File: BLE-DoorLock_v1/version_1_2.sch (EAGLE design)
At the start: 33 parts, among them K1 G5LE-14_DC12, Q1 MMBT2222, Q2 MMBT2222, Q3 DMN6140L

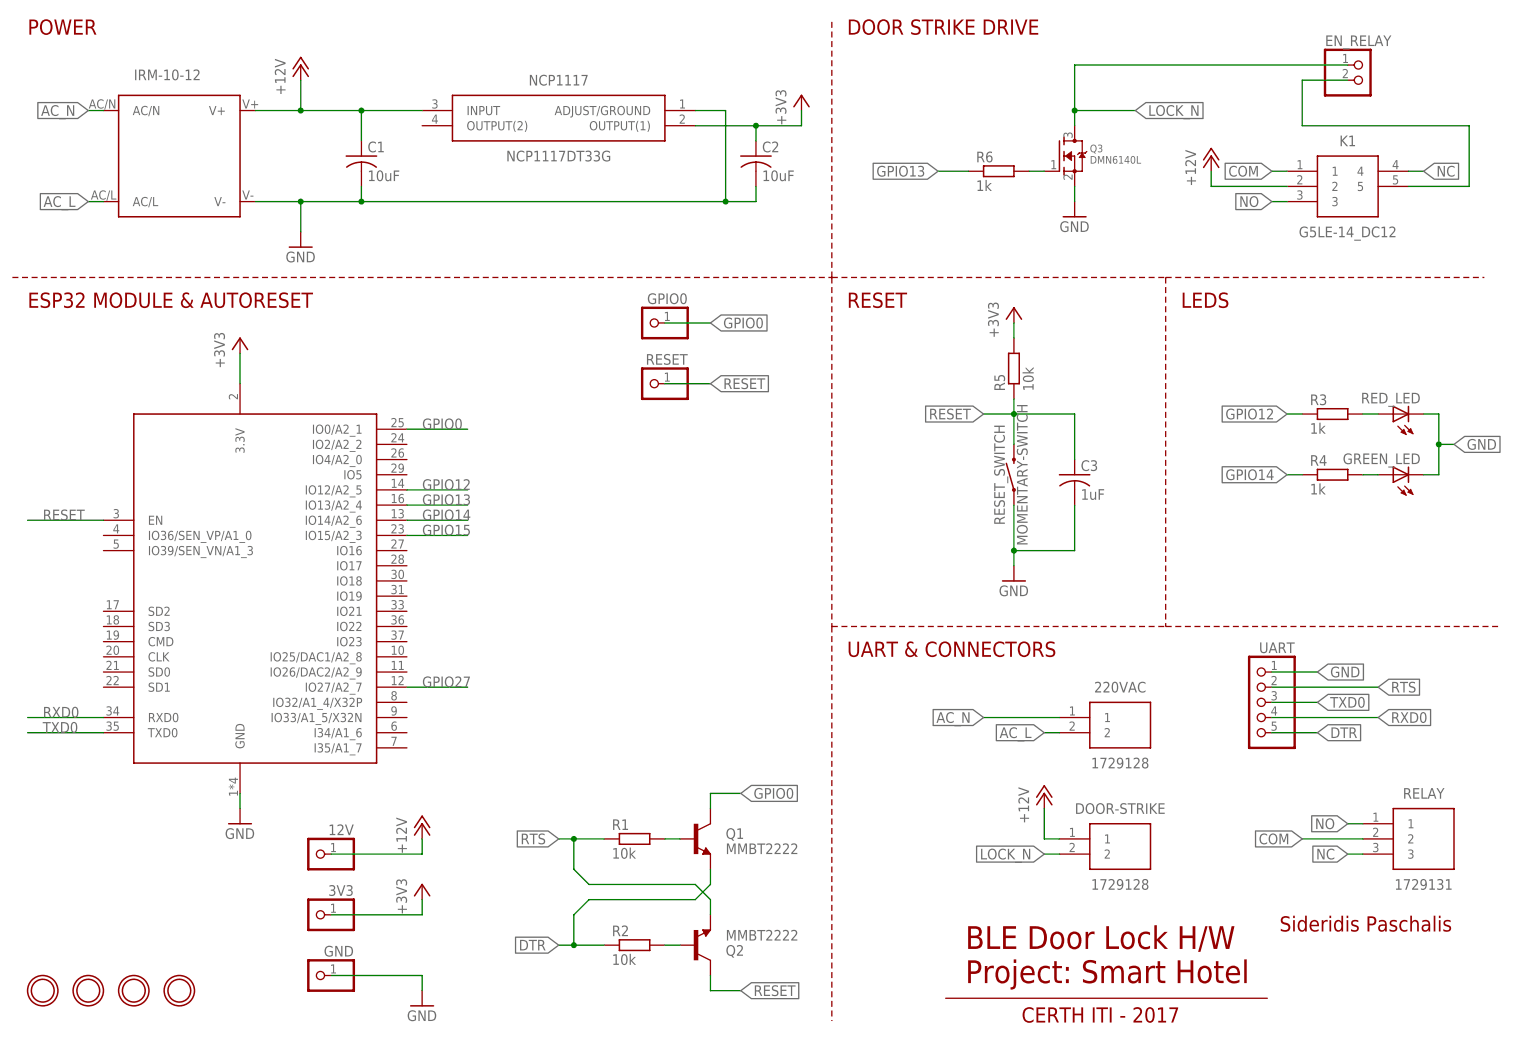
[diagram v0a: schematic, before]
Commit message: Demo PCB -with relay- version_1.2
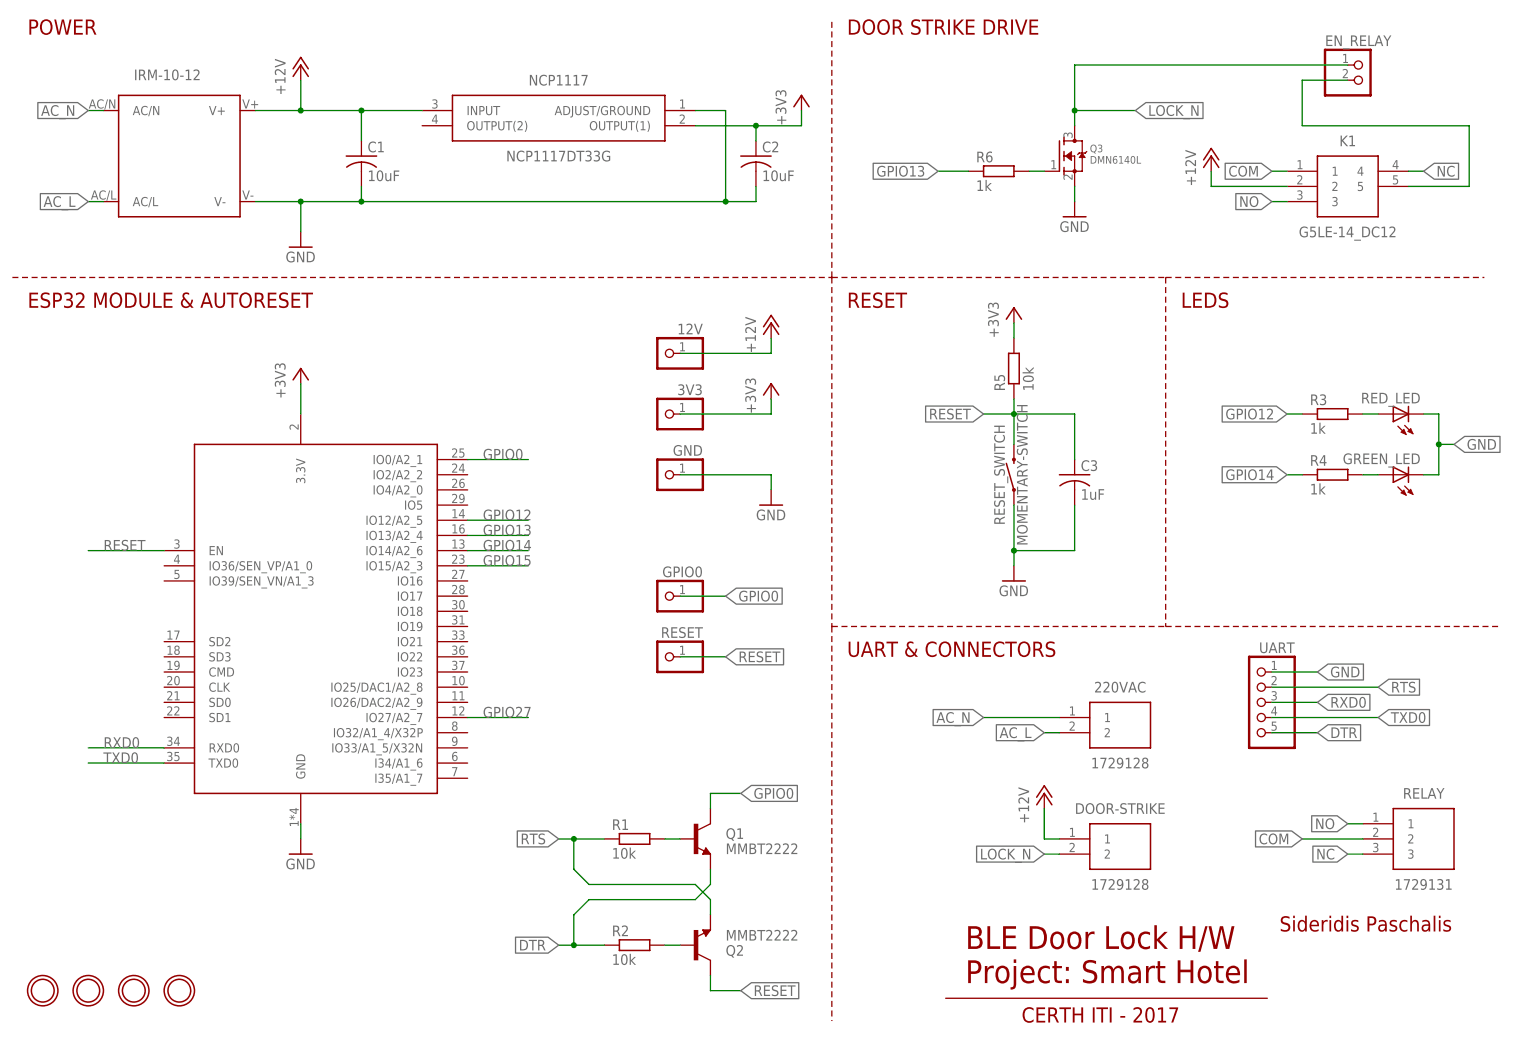
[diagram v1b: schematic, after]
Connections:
- net RXD0: now also UART.3; no longer UART.4
- net TXD0: now also UART.4; no longer UART.3
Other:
- moved on the sheet: 12V, 3V3, GND, GPIO0, RESET
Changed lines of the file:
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@@
 <instances>
 <instance part="FRAME1" gate="G$1" x="0" y="0"/>
-<instance part="ESP32" gate="G$1" x="43.18" y="71.12"/>
+<instance part="ESP32" gate="G$1" x="53.34" y="66.04"/>
 <instance part="IRM-10-12" gate="G$1" x="33.02" y="149.86"/>
 <instance part="NCP1117" gate="G$1" x="119.38" y="157.48" rot="MR0"/>
@@
 <instance part="R1" gate="G$1" x="109.22" y="35.56"/>
 <instance part="R2" gate="G$1" x="109.22" y="17.78"/>
-<instance part="GND2" gate="1" x="43.18" y="38.1"/>
-<instance part="+3V2" gate="G$1" x="43.18" y="119.38"/>
+<instance part="GND2" gate="1" x="53.34" y="33.02"/>
+<instance part="+3V2" gate="G$1" x="53.34" y="114.3"/>
 <instance part="RED_LED" gate="G$1" x="236.22" y="106.68" rot="R90"/>
 <instance part="GREEN_LED" gate="G$1" x="236.22" y="96.52" rot="R90"/>
@@
 <instance part="C2" gate="G$1" x="129.54" y="149.86"/>
 <instance part="C3" gate="G$1" x="182.88" y="96.52"/>
-<instance part="12V" gate="G$1" x="55.88" y="33.02" rot="MR0"/>
-<instance part="3V3" gate="G$1" x="55.88" y="22.86" rot="MR0"/>
-<instance part="GND" gate="G$1" x="55.88" y="12.7" rot="MR0"/>
-<instance part="P+3" gate="1" x="73.66" y="38.1"/>
-<instance part="+3V4" gate="G$1" x="73.66" y="27.94"/>
-<instance part="GND5" gate="1" x="73.66" y="7.62"/>
-<instance part="GPIO0" gate="G$1" x="111.76" y="121.92" rot="MR0"/>
-<instance part="RESET" gate="G$1" x="111.76" y="111.76" rot="MR0"/>
+<instance part="12V" gate="G$1" x="114.3" y="116.84" rot="MR0"/>
+<instance part="3V3" gate="G$1" x="114.3" y="106.68" rot="MR0"/>
+<instance part="GND" gate="G$1" x="114.3" y="96.52" rot="MR0"/>
+<instance part="P+3" gate="1" x="132.08" y="121.92"/>
+<instance part="+3V4" gate="G$1" x="132.08" y="111.76"/>
+<instance part="GND5" gate="1" x="132.08" y="91.44"/>
+<instance part="GPIO0" gate="G$1" x="114.3" y="76.2" rot="MR0"/>
+<instance part="RESET" gate="G$1" x="114.3" y="66.04" rot="MR0"/>
 <instance part="U$1" gate="G$1" x="10.16" y="10.16"/>
 <instance part="U$2" gate="G$1" x="17.78" y="10.16"/>
@@
 <pinref part="12V" gate="G$1" pin="1"/>
 <pinref part="P+3" gate="1" pin="+12V"/>
-<wire x1="58.42" y1="33.02" x2="73.66" y2="33.02" width="0.1524" layer="91"/>
-<wire x1="73.66" y1="33.02" x2="73.66" y2="35.56" width="0.1524" layer="91"/>
+<wire x1="116.84" y1="116.84" x2="132.08" y2="116.84" width="0.1524" layer="91"/>
+<wire x1="132.08" y1="116.84" x2="132.08" y2="119.38" width="0.1524" layer="91"/>
 </segment>
 <segment>
@@
 <pinref part="GND2" gate="1" pin="GND"/>
 <pinref part="ESP32" gate="G$1" pin="GND"/>
-<wire x1="43.18" y1="40.64" x2="43.18" y2="43.18" width="0.1524" layer="91"/>
+<wire x1="53.34" y1="35.56" x2="53.34" y2="38.1" width="0.1524" layer="91"/>
 </segment>
 <segment>
@@
 <pinref part="GND" gate="G$1" pin="1"/>
 <pinref part="GND5" gate="1" pin="GND"/>
-<wire x1="58.42" y1="12.7" x2="73.66" y2="12.7" width="0.1524" layer="91"/>
-<wire x1="73.66" y1="12.7" x2="73.66" y2="10.16" width="0.1524" layer="91"/>
+<wire x1="116.84" y1="96.52" x2="132.08" y2="96.52" width="0.1524" layer="91"/>
+<wire x1="132.08" y1="96.52" x2="132.08" y2="93.98" width="0.1524" layer="91"/>
 </segment>
 </net>
@@
 <pinref part="ESP32" gate="G$1" pin="3.3V"/>
 <pinref part="+3V2" gate="G$1" pin="+3V3"/>
-<wire x1="43.18" y1="111.76" x2="43.18" y2="116.84" width="0.1524" layer="91"/>
+<wire x1="53.34" y1="106.68" x2="53.34" y2="111.76" width="0.1524" layer="91"/>
 </segment>
 <segment>
@@
 <pinref part="3V3" gate="G$1" pin="1"/>
 <pinref part="+3V4" gate="G$1" pin="+3V3"/>
-<wire x1="58.42" y1="22.86" x2="73.66" y2="22.86" width="0.1524" layer="91"/>
-<wire x1="73.66" y1="22.86" x2="73.66" y2="25.4" width="0.1524" layer="91"/>
+<wire x1="116.84" y1="106.68" x2="132.08" y2="106.68" width="0.1524" layer="91"/>
+<wire x1="132.08" y1="106.68" x2="132.08" y2="109.22" width="0.1524" layer="91"/>
 </segment>
 </net>
@@
 <segment>
 <pinref part="ESP32" gate="G$1" pin="IO0/A2_1"/>
-<wire x1="71.12" y1="104.14" x2="81.28" y2="104.14" width="0.1524" layer="91"/>
-<label x="73.66" y="104.14" size="1.778" layer="95"/>
+<wire x1="81.28" y1="99.06" x2="91.44" y2="99.06" width="0.1524" layer="91"/>
+<label x="83.82" y="99.06" size="1.778" layer="95"/>
 </segment>
 <segment>
 <pinref part="GPIO0" gate="G$1" pin="1"/>
-<wire x1="114.3" y1="121.92" x2="121.92" y2="121.92" width="0.1524" layer="91"/>
-<label x="121.92" y="121.92" size="1.778" layer="95" xref="yes"/>
+<wire x1="116.84" y1="76.2" x2="124.46" y2="76.2" width="0.1524" layer="91"/>
+<label x="124.46" y="76.2" size="1.778" layer="95" xref="yes"/>
 </segment>
 </net>
@@
 <segment>
 <pinref part="ESP32" gate="G$1" pin="EN"/>
-<wire x1="20.32" y1="88.9" x2="7.62" y2="88.9" width="0.1524" layer="91"/>
-<label x="10.16" y="88.9" size="1.778" layer="95"/>
+<wire x1="30.48" y1="83.82" x2="17.78" y2="83.82" width="0.1524" layer="91"/>
+<label x="20.32" y="83.82" size="1.778" layer="95"/>
 </segment>
 <segment>
@@
 <segment>
 <pinref part="RESET" gate="G$1" pin="1"/>
-<wire x1="114.3" y1="111.76" x2="121.92" y2="111.76" width="0.1524" layer="91"/>
-<label x="121.92" y="111.76" size="1.778" layer="95" xref="yes"/>
+<wire x1="116.84" y1="66.04" x2="124.46" y2="66.04" width="0.1524" layer="91"/>
+<label x="124.46" y="66.04" size="1.778" layer="95" xref="yes"/>
 </segment>
 </net>
@@
 <segment>
 <pinref part="ESP32" gate="G$1" pin="IO15/A2_3"/>
-<wire x1="71.12" y1="86.36" x2="81.28" y2="86.36" width="0.1524" layer="91"/>
-<label x="73.66" y="86.36" size="1.778" layer="95"/>
+<wire x1="81.28" y1="81.28" x2="91.44" y2="81.28" width="0.1524" layer="91"/>
+<label x="83.82" y="81.28" size="1.778" layer="95"/>
 </segment>
 </net>
@@
 <segment>
 <pinref part="ESP32" gate="G$1" pin="IO14/A2_6"/>
-<wire x1="71.12" y1="88.9" x2="81.28" y2="88.9" width="0.1524" layer="91"/>
-<label x="73.66" y="88.9" size="1.778" layer="95"/>
+<wire x1="81.28" y1="83.82" x2="91.44" y2="83.82" width="0.1524" layer="91"/>
+<label x="83.82" y="83.82" size="1.778" layer="95"/>
 </segment>
 <segment>
@@
 <segment>
 <pinref part="ESP32" gate="G$1" pin="RXD0"/>
-<wire x1="20.32" y1="55.88" x2="7.62" y2="55.88" width="0.1524" layer="91"/>
-<label x="10.16" y="55.88" size="1.778" layer="95"/>
-</segment>
-<segment>
+<wire x1="30.48" y1="50.8" x2="17.78" y2="50.8" width="0.1524" layer="91"/>
+<label x="20.32" y="50.8" size="1.778" layer="95"/>
+</segment>
+<segment>
+<pinref part="UART" gate="A" pin="3"/>
+<wire x1="215.9" y1="58.42" x2="223.52" y2="58.42" width="0.1524" layer="91"/>
+<label x="223.52" y="58.42" size="1.778" layer="95" xref="yes"/>
+</segment>
+</net>
+<net name="TXD0" class="0">
+<segment>
+<pinref part="ESP32" gate="G$1" pin="TXD0"/>
+<wire x1="30.48" y1="48.26" x2="17.78" y2="48.26" width="0.1524" layer="91"/>
+<label x="20.32" y="48.26" size="1.778" layer="95"/>
+</segment>
+<segment>
+<pinref part="UART" gate="A" pin="4"/>
 <wire x1="215.9" y1="55.88" x2="233.68" y2="55.88" width="0.1524" layer="91"/>
 <label x="233.68" y="55.88" size="1.778" layer="95" xref="yes"/>
-<pinref part="UART" gate="A" pin="4"/>
-</segment>
-</net>
-<net name="TXD0" class="0">
-<segment>
-<pinref part="ESP32" gate="G$1" pin="TXD0"/>
-<wire x1="20.32" y1="53.34" x2="7.62" y2="53.34" width="0.1524" layer="91"/>
-<label x="10.16" y="53.34" size="1.778" layer="95"/>
-</segment>
-<segment>
-<label x="223.52" y="58.42" size="1.778" layer="95" xref="yes"/>
-<pinref part="UART" gate="A" pin="3"/>
-<wire x1="223.52" y1="58.42" x2="215.9" y2="58.42" width="0.1524" layer="91"/>
 </segment>
 </net>
@@
 <segment>
 <pinref part="ESP32" gate="G$1" pin="IO27/A2_7"/>
-<wire x1="71.12" y1="60.96" x2="81.28" y2="60.96" width="0.1524" layer="91"/>
-<label x="73.66" y="60.96" size="1.778" layer="95"/>
+<wire x1="81.28" y1="55.88" x2="91.44" y2="55.88" width="0.1524" layer="91"/>
+<label x="83.82" y="55.88" size="1.778" layer="95"/>
 </segment>
 </net>
@@
 <segment>
 <pinref part="ESP32" gate="G$1" pin="IO12/A2_5"/>
-<wire x1="71.12" y1="93.98" x2="81.28" y2="93.98" width="0.1524" layer="91"/>
-<label x="73.66" y="93.98" size="1.778" layer="95"/>
+<wire x1="81.28" y1="88.9" x2="91.44" y2="88.9" width="0.1524" layer="91"/>
+<label x="83.82" y="88.9" size="1.778" layer="95"/>
 </segment>
 <segment>
@@
 <segment>
 <pinref part="ESP32" gate="G$1" pin="IO13/A2_4"/>
-<wire x1="71.12" y1="91.44" x2="81.28" y2="91.44" width="0.1524" layer="91"/>
-<label x="73.66" y="91.44" size="1.778" layer="95"/>
-</segment>
-<segment>
+<wire x1="81.28" y1="86.36" x2="91.44" y2="86.36" width="0.1524" layer="91"/>
+<label x="83.82" y="86.36" size="1.778" layer="95"/>
+</segment>
+<segment>
